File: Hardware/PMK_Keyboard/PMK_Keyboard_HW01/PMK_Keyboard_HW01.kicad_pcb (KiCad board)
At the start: 2 copper layers, 181.6 x 172.3 mm, 151 parts, among them J101 USB4510-03-1-A, J401 Conn_01x08_Female, J402 Conn_01x03_Socket, SW501 SW_Push, SW502 SW_Push, SW503 SW_Push, SW504 SW_Push, SW505 SW_Push, SW506 SW_Push, SW507 SW_Push, SW508 SW_Push, SW509 SW_Push, SW510 SW_Push, SW511 SW_Push, SW512 SW_Push, SW513 SW_Push, SW514 SW_Push, SW515 SW_Push, SW516 SW_Push, SW517 SW_Push, SW518 SW_Push, SW519 SW_Push, SW520 SW_Push, SW521 SW_Push, SW522 SW_Push, SW523 SW_Push, SW524 SW_Push, SW525 SW_Push, SW526 SW_Push, SW527 SW_Push, SW528 SW_Push, SW529 SW_Push, SW530 SW_Push, SW531 SW_Push, SW532 SW_Push, SW533 SW_Push, SW534 SW_Push, SW535 SW_Push, SW536 SW_Push, SW537 SW_Push, SW538 SW_Push, SW539 SW_Push, SW540 SW_Push, U201 BQ24075RGTR, U301 MIC5528-3.3YMT-T5, U302 MIC5528-3.3YMT-T5, U401 ESP32-S2FH4, U501 SN74HC165PWR, U502 SN74HC165PWR, U503 SN74HC165PWR, U504 SN74HC165PWR, U505 SN74HC165PWR, Y601 Crystal_GND24_Small

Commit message: Started routing
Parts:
- removed ANT401: 2450AT18A100E, Component_lib:ANTC3216X140N
- removed BT101: Battery_Cell, Component_lib:BatteryHolder_Keystone_1042_1x18650_DUALSIDE
- removed C201, C203: 4u7, Capacitor_SMD:C_0603_1608Metric
- removed C202: 1u, Capacitor_SMD:C_0603_1608Metric
- removed C301, C302, C303, C304: 2u2, Capacitor_SMD:C_0603_1608Metric
- removed C401, C402: 15p, Capacitor_SMD:C_0201_0603Metric
- removed C403, C404, C405, C408, C411, C412, C414, C415, C416: 100n, Capacitor_SMD:C_0402_1005Metric
- removed C406, C407: C, Capacitor_SMD:C_0201_0603Metric
- removed C409: 10u, Capacitor_SMD:C_0603_1608Metric
- removed C410, C413: 1u, Capacitor_SMD:C_0402_1005Metric
- removed D201, D202: LED, Component_lib:LED_0402_1005Metric_DUALSIDE
- removed D601, D602, D603, D604, D605, D606, D607, D608, D609, D610, D611, D612, D613, D614, D615, D616, D617, D618, D619, D620, D621, D622, D623, D624, D625, D626, D627, D628, D629, D630, D631, D632, D633, D634, D635, D636, D637, D638, D639, D640: YF923_2020_WS2812_LED, Component_lib:YF923_2020_WS2812_LED_DUALSIDE
- removed G*** (x2): LOGO, Component_lib:puma_logo_14mm
- removed G***: LOGO, Component_lib:pmk-v1-noFN_180mm
- removed J401: Conn_01x08_Female, Connector_PinHeader_1.27mm:PinHeader_1x08_P1.27mm_Vertical
- removed J402: Conn_01x03_Socket, Connector_PinHeader_2.54mm:PinHeader_1x03_P2.54mm_Vertical
- removed L401: L, Inductor_SMD:L_0201_0603Metric
- removed R205, R206: 1k5, Resistor_SMD:R_0402_1005Metric
- removed R207: 100k, Resistor_SMD:R_0402_1005Metric
- removed R301: 0k, Resistor_SMD:R_0201_0603Metric
- removed R401: 0, Resistor_SMD:R_0201_0603Metric
- removed R402: 2k, Resistor_SMD:R_0402_1005Metric
- removed R403, R404: 10k, Resistor_SMD:R_0201_0603Metric
- removed R405, R406, R407, R408: nu, Resistor_SMD:R_0201_0603Metric
- removed RN501, RN502, RN503, RN504, RN505: EXB-2HV103JV, Component_lib:EXB2HV_1
- removed S401, S402: SKRPABE010, Component_lib:SKRPABE010
- removed SW501: SW_Push, Component_lib:SKRPABE010
- removed SW502, SW503, SW504, SW505, SW506, SW507, SW508, SW509, SW510, SW511, SW512, SW513, SW514, SW515, SW516, SW517, SW518, SW519, SW520, SW521, SW522, SW523, SW524, SW525, SW526, SW527, SW528, SW529, SW530, SW531, SW532, SW533, SW534, SW535, SW536, SW537, SW538, SW539, SW540: SW_Push, Component_lib:Kailh_socket_PG1350_reversible
- removed TP201: TestPoint, TestPoint:TestPoint_Pad_D1.0mm
- removed U201: BQ24075RGTR, Component_lib:QFN50P300X300X100-17N-D
- removed U401: ESP32-S2FH4, Component_lib:QFN40P700X700X90-57N-D
- removed U501, U502, U503, U504, U505: SN74HC165PWR, Component_lib:SOP65P640X120-16N
- removed Y601: Crystal_GND24_Small, Component_lib:Crystal_SMD_2016-4Pin_2.0x1.6mm
- added D402: YF923_2020_WS2812_LED, Component_lib:YF923_2020_WS2812_LED_DUALSIDE, F.Cu at (43.9, 80.0)
- added D403: YF923_2020_WS2812_LED, Component_lib:YF923_2020_WS2812_LED_DUALSIDE, F.Cu at (43.9, 83.6)
- added D404: YF923_2020_WS2812_LED, Component_lib:YF923_2020_WS2812_LED_DUALSIDE, F.Cu at (43.9, 87.1)
- added D405: YF923_2020_WS2812_LED, Component_lib:YF923_2020_WS2812_LED_DUALSIDE, F.Cu at (43.9, 90.7)
- added D406: YF923_2020_WS2812_LED, Component_lib:YF923_2020_WS2812_LED_DUALSIDE, F.Cu at (43.9, 94.2)
- added D407: YF923_2020_WS2812_LED, Component_lib:YF923_2020_WS2812_LED_DUALSIDE, F.Cu at (43.9, 97.8)
- added D408: YF923_2020_WS2812_LED, Component_lib:YF923_2020_WS2812_LED_DUALSIDE, F.Cu at (43.9, 101.3)
- added D409: YF923_2020_WS2812_LED, Component_lib:YF923_2020_WS2812_LED_DUALSIDE, F.Cu at (43.9, 104.8)
- added D410: YF923_2020_WS2812_LED, Component_lib:YF923_2020_WS2812_LED_DUALSIDE, F.Cu at (48.5, 76.5)
- added D411: YF923_2020_WS2812_LED, Component_lib:YF923_2020_WS2812_LED_DUALSIDE, F.Cu at (48.5, 80.0)
- added D412: YF923_2020_WS2812_LED, Component_lib:YF923_2020_WS2812_LED_DUALSIDE, F.Cu at (48.5, 83.6)
- added D413: YF923_2020_WS2812_LED, Component_lib:YF923_2020_WS2812_LED_DUALSIDE, F.Cu at (48.5, 87.1)
- added D414: YF923_2020_WS2812_LED, Component_lib:YF923_2020_WS2812_LED_DUALSIDE, F.Cu at (48.5, 90.7)
- added D415: YF923_2020_WS2812_LED, Component_lib:YF923_2020_WS2812_LED_DUALSIDE, F.Cu at (48.5, 94.2)
- added D416: YF923_2020_WS2812_LED, Component_lib:YF923_2020_WS2812_LED_DUALSIDE, F.Cu at (48.5, 97.8)
- added D417: YF923_2020_WS2812_LED, Component_lib:YF923_2020_WS2812_LED_DUALSIDE, F.Cu at (48.5, 101.3)
- added D418: YF923_2020_WS2812_LED, Component_lib:YF923_2020_WS2812_LED_DUALSIDE, F.Cu at (48.5, 104.8)
- added D419: YF923_2020_WS2812_LED, Component_lib:YF923_2020_WS2812_LED_DUALSIDE, F.Cu at (53.1, 76.5)
- added D420: YF923_2020_WS2812_LED, Component_lib:YF923_2020_WS2812_LED_DUALSIDE, F.Cu at (53.1, 80.0)
- added D421: YF923_2020_WS2812_LED, Component_lib:YF923_2020_WS2812_LED_DUALSIDE, F.Cu at (53.1, 83.6)
- added D422: YF923_2020_WS2812_LED, Component_lib:YF923_2020_WS2812_LED_DUALSIDE, F.Cu at (53.1, 87.1)
- added D423: YF923_2020_WS2812_LED, Component_lib:YF923_2020_WS2812_LED_DUALSIDE, F.Cu at (53.1, 90.7)
- added D424: YF923_2020_WS2812_LED, Component_lib:YF923_2020_WS2812_LED_DUALSIDE, F.Cu at (53.1, 94.2)
- added D425: YF923_2020_WS2812_LED, Component_lib:YF923_2020_WS2812_LED_DUALSIDE, F.Cu at (53.1, 97.8)
- added D426: YF923_2020_WS2812_LED, Component_lib:YF923_2020_WS2812_LED_DUALSIDE, F.Cu at (53.1, 101.3)
- added D427: YF923_2020_WS2812_LED, Component_lib:YF923_2020_WS2812_LED_DUALSIDE, F.Cu at (53.1, 104.8)
- added D428: YF923_2020_WS2812_LED, Component_lib:YF923_2020_WS2812_LED_DUALSIDE, F.Cu at (57.8, 76.5)
- added D429: YF923_2020_WS2812_LED, Component_lib:YF923_2020_WS2812_LED_DUALSIDE, F.Cu at (57.8, 80.0)
- added D430: YF923_2020_WS2812_LED, Component_lib:YF923_2020_WS2812_LED_DUALSIDE, F.Cu at (57.8, 83.6)
- added D431: YF923_2020_WS2812_LED, Component_lib:YF923_2020_WS2812_LED_DUALSIDE, F.Cu at (57.8, 87.1)
- added D432: YF923_2020_WS2812_LED, Component_lib:YF923_2020_WS2812_LED_DUALSIDE, F.Cu at (57.8, 90.7)
- added J102: PSoM_ESP32S2_Carrier_Board, Component_lib:PSoM_ESP32S2_00, F.Cu at (209.4, 64.8)
- added J201: USB4510-03-1-A, Component_lib:USB4510031A, F.Cu at (209.1, 56.7)
- added J202: Conn_01x05_Pin, Component_lib:SMD_CONN_01x5_1.5mm, B.Cu at (217.4, 89.7)
- added J203: Cirque, Component_lib:Cirque trackpad, F.Cu at (218.8, 89.7)
- added J204: S2B-PH-SM4-TB, Component_lib:JST_PH_B2B-PH-SM4-TB_1x02-1MP_P2.00mm_Vertical_DUALSIDE, F.Cu at (209.2, 89.3)
- added RN301: EXB-2HV103JV, Component_lib:EXB2HV_1, F.Cu at (197.7, 93.6)
- added RN302: EXB-2HV103JV, Component_lib:EXB2HV_1, F.Cu at (197.7, 90.2)
- added RN303: EXB-2HV103JV, Component_lib:EXB2HV_1, F.Cu at (197.7, 86.8)
- added RN304: EXB-2HV103JV, Component_lib:EXB2HV_1, F.Cu at (197.7, 83.4)
- added SW201: 450405020524, Component_lib:450405020524_DUALSIDE, F.Cu at (195.8, 57.5)
- added SW301: RIC11-22S10D5S-TH, Component_lib:RIC11-22S10D5S-TH, F.Cu at (217.1, 126.5)
- added SW302: SW_Push, Component_lib:Kailh_socket_PG1350_reversible, F.Cu at (93.0, 69.1)
- added SW303: SW_Push, Component_lib:Kailh_socket_PG1350_reversible, F.Cu at (112.1, 69.1)
- added SW304: SW_Push, Component_lib:Kailh_socket_PG1350_reversible, F.Cu at (131.1, 64.2)
- added SW305: SW_Push, Component_lib:Kailh_socket_PG1350_reversible, F.Cu at (150.2, 61.4)
- added SW306: SW_Push, Component_lib:Kailh_socket_PG1350_reversible, F.Cu at (169.2, 64.2)
- added SW307: SW_Push, Component_lib:Kailh_socket_PG1350_reversible, F.Cu at (188.3, 66.7)
- added SW308: SW_Push, Component_lib:Kailh_socket_PG1350_reversible, F.Cu at (93.0, 88.2)
- added SW309: SW_Push, Component_lib:Kailh_socket_PG1350_reversible, F.Cu at (112.1, 88.2)
- added SW310: SW_Push, Component_lib:Kailh_socket_PG1350_reversible, F.Cu at (131.1, 83.3)
- added SW311: SW_Push, Component_lib:Kailh_socket_PG1350_reversible, F.Cu at (150.2, 80.8)
- added SW312: SW_Push, Component_lib:Kailh_socket_PG1350_reversible, F.Cu at (169.2, 83.3)
- added SW313: SW_Push, Component_lib:Kailh_socket_PG1350_reversible, F.Cu at (188.3, 85.8)
- added SW314: SW_Push, Component_lib:Kailh_socket_PG1350_reversible, F.Cu at (93.0, 107.2)
- added SW315: SW_Push, Component_lib:Kailh_socket_PG1350_reversible, F.Cu at (112.1, 107.2)
- added SW316: SW_Push, Component_lib:Kailh_socket_PG1350_reversible, F.Cu at (131.1, 102.3)
- added SW317: SW_Push, Component_lib:Kailh_socket_PG1350_reversible, F.Cu at (150.2, 99.8)
- added SW318: SW_Push, Component_lib:Kailh_socket_PG1350_reversible, F.Cu at (169.2, 102.3)
- added SW319: SW_Push, Component_lib:Kailh_socket_PG1350_reversible, F.Cu at (188.3, 104.8)
- added SW320: SW_Push, Component_lib:Kailh_socket_PG1350_reversible, F.Cu at (93.0, 126.3)
- added SW321: SW_Push, Component_lib:Kailh_socket_PG1350_reversible, F.Cu at (112.1, 126.3)
- added SW322: SW_Push, Component_lib:Kailh_socket_PG1350_reversible, F.Cu at (131.1, 121.4)
- added SW323: SW_Push, Component_lib:Kailh_socket_PG1350_reversible, F.Cu at (150.2, 118.9)
- added SW324: SW_Push, Component_lib:Kailh_socket_PG1350_reversible, F.Cu at (169.2, 121.4)
- added SW325: SW_Push, Component_lib:Kailh_socket_PG1350_reversible, F.Cu at (188.3, 123.9)
- added SW326: SW_Push, Component_lib:Kailh_socket_PG1350_reversible, F.Cu at (131.1, 140.4)
- added SW327: SW_Push, Component_lib:Kailh_socket_PG1350_reversible, F.Cu at (150.2, 137.9)
- added SW328: SW_Push, Component_lib:Kailh_socket_PG1350_reversible, F.Cu at (169.2, 140.4)
- added SW329: SW_Push, Component_lib:Kailh_socket_PG1350_reversible, F.Cu at (191.2, 145.1)
- added SW330: SW_Push, Component_lib:Kailh_socket_PG1350_reversible, F.Cu at (212.1, 150.1)
- added TH101: Thermistor_NTC, Resistor_SMD:R_0402_1005Metric, F.Cu at (159.8, 93.8)
- added U303: SN74HC165PWR, Component_lib:SOP65P640X120-16N, F.Cu at (195.8, 112.0)
- added U304: SN74HC165PWR, Component_lib:SOP65P640X120-16N, F.Cu at (195.8, 105.2)
- D401: value LED -> YF923_2020_WS2812_LED; footprint Component_lib:LED_0402_1005Metric_DUALSIDE -> Component_lib:YF923_2020_WS2812_LED_DUALSIDE
- J101: value USB4510-03-1-A -> PSoM_ESP32S2_Carrier_Board; footprint Component_lib:USB4510031A -> Component_lib:PSoM_ESP32S2_00; moved to B.Cu
- R101, R102: value 5.1k -> R; footprint Resistor_SMD:R_0201_0603Metric -> Resistor_SMD:R_0402_1005Metric
- R201: value 0 -> 5.1k; footprint Resistor_SMD:R_0402_1005Metric -> Resistor_SMD:R_0201_0603Metric
- R202: value 36k5 -> 5.1k; footprint Resistor_SMD:R_0402_1005Metric -> Resistor_SMD:R_0201_0603Metric
- R203: value 590 -> 0; footprint Resistor_SMD:R_0402_1005Metric -> Resistor_SMD:R_0201_0603Metric
- R204: value 1k1 -> 0; footprint Resistor_SMD:R_0402_1005Metric -> Resistor_SMD:R_0201_0603Metric
- U301, U302: value MIC5528-3.3YMT-T5 -> SN74HC165PWR; footprint Component_lib:SON40P120X120X60-7N-D -> Component_lib:SOP65P640X120-16N
- moved R203 132.6 mm to (112.0, 143.9)
- moved R204 129.5 mm to (113.3, 145.1), turned to 45 degrees
- moved R202 128.5 mm to (108.3, 140.1)
- moved R201 128.1 mm to (107.1, 138.9)
- moved D401 120.1 mm to (43.9, 76.5), turned to 0 degrees
- moved U302 109.3 mm to (195.8, 118.7), turned to 180 degrees
- moved R101 96.3 mm to (205.5, 88.5), turned to 0 degrees
- moved R102 94.7 mm to (205.5, 90.5), turned to 0 degrees
- moved J101 84.8 mm to (209.3, 64.8), turned to 0 degrees
- moved U301 81.4 mm to (209.5, 73.6), turned to 180 degrees
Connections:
- D401 pad 2: /400- ESP32S2FH4S2/LED_NET -> VDD
- R101 pad 1: /100- Connectors/CC2 -> /100- PSoM/LED_MOSI_ESP
- R101 pad 2: GND -> /100- PSoM/LED_MOSI
- R102 pad 1: /100- Connectors/CC1 -> /100- PSoM/SPI_CLK_ESP
- R102 pad 2: GND -> /100- PSoM/SPI_MISO
- R201 pad 1: /200- 1S_Charger/SYSOFF -> /200- Connectors/CC2
- R202 pad 1: /200- 1S_Charger/TMR -> /200- Connectors/CC1
- R203 pad 1: /200- 1S_Charger/ISET -> Net-(SW201-A)
- R203 pad 2: GND -> /VBAT
- R204 pad 1: GND -> Net-(SW201-C)
- R204 pad 2: /200- 1S_Charger/ILIM -> /VBAT
- U301 pad 1: +3V3 -> /100- PSoM/PL
- U301 pad 2: +3V3 -> /100- PSoM/SPI_CLK
- U301 pad 3: GND -> /300- Shift Register - Switch/4
- U301 pad 4: /300- Power/PRIM_LDO_EN -> /300- Shift Register - Switch/3
- U301 pad 5: unconnected-(U301-NC-Pad5) -> /300- Shift Register - Switch/2
- U301 pad 6: /VSYS -> /300- Shift Register - Switch/1
- U301 pad 7: GND -> unconnected-(U301-~{QH}-Pad7)
- U302 pad 1: VDD -> /100- PSoM/PL
- U302 pad 2: VDD -> /100- PSoM/SPI_CLK
- U302 pad 3: GND -> /300- Shift Register - Switch/12
- U302 pad 4: /300- Power/LED_EN -> /300- Shift Register - Switch/11
- U302 pad 5: unconnected-(U302-NC-Pad5) -> /300- Shift Register - Switch/10
- U302 pad 6: /VSYS -> /300- Shift Register - Switch/9
- U302 pad 7: GND -> unconnected-(U302-~{QH}-Pad7)
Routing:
- net VDD: track 1246.0 -> 0.00 mm, vias 53 -> 0
- net GND: track 388.5 -> 0.00 mm, vias 151 -> 0
- net +3V3: track 227.7 -> 0.00 mm, vias 19 -> 0
- net /500- Shift Register - Switch/18: track 178.7 -> 0.00 mm, vias 2 -> 0
- net /400- ESP32S2FH4S2/SR_CLK: track 176.9 -> 0.00 mm, vias 7 -> 0
- net /500- Shift Register - Switch/17: track 174.3 -> 0.00 mm, vias 2 -> 0
- net /400- ESP32S2FH4S2/SR_CS: track 173.7 -> 0.00 mm, vias 8 -> 0
- net /500- Shift Register - Switch/10: track 172.6 -> 0.00 mm, vias 4 -> 0
- net /500- Shift Register - Switch/25: track 170.7 -> 0.00 mm, vias 2 -> 0
- net /400- ESP32S2FH4S2/PL: track 158.6 -> 0.00 mm, vias 7 -> 0
- net /500- Shift Register - Switch/2: track 158.4 -> 0.00 mm, vias 2 -> 0
- net /500- Shift Register - Switch/9: track 156.5 -> 0.00 mm, vias 2 -> 0
- net /500- Shift Register - Switch/27: track 155.4 -> 0.00 mm, vias 2 -> 0
- net /500- Shift Register - Switch/26: track 154.3 -> 0.00 mm, vias 2 -> 0
- net /500- Shift Register - Switch/19: track 134.6 -> 0.00 mm, vias 2 -> 0
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- removed copper zone on B.Cu, net +3V3
- removed copper zone on F.Cu, net +3V3
- removed copper zone on F.Cu, net /VSYS
- removed copper zone on B.Cu, net GND
- removed copper zone on F.Cu, net GND
- removed copper zone on F.Cu, net VDD
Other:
- board size 181.6 x 172.3 mm -> 143.4 x 111.7 mm
- board text added: "+"
- board text added: "-"
- board text added: "Sofle Choc Wireless - revision by db"
- board text added: "s1"
- board text added: "s10"
- board text added: "s11"
- board text added: "s12"
- board text added: "s13"
- board text added: "s14"
- board text added: "s15"
- board text added: "s16"
- board text added: "s17"
- board text added: "s18"
- board text added: "s19"
- board text added: "s2"
- board text added: "s20"
- board text added: "s21"
- board text added: "s22"
- board text added: "s23"
- board text added: "s24"
- board text added: "s25"
- board text added: "s26"
- board text added: "s27"
- board text added: "s28"
- board text added: "s29"
- board text added: "s3"
- board text added: "s30"
- board text added: "s4"
- board text added: "s5"
- board text added: "s6"
- board text added: "s7"
- board text added: "s8"
- board text added: "s9"
- board text removed: "PMK_KEYBOARD_HW00"

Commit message: working on routing
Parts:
- removed D430, D431, D432: YF923_2020_WS2812_LED, Component_lib:YF923_2020_WS2812_LED_DUALSIDE
- removed the SW301 at (217.1, 126.5)
- added SW330: RIC11-22S10D5S-TH, Component_lib:RIC11-22S10D5S-TH, F.Cu at (214.8, 126.8)
- J202: moved to F.Cu
- J203, RN301, RN302, RN303, RN304: moved to B.Cu
- J204: footprint Component_lib:JST_PH_B2B-PH-SM4-TB_1x02-1MP_P2.00mm_Vertical_DUALSIDE -> Component_lib:JST_PH_S2B-PH-SM4-TB_1x02-1MP_P2.00mm_Horizontal_DUALSIDE; moved to B.Cu
- moved D425 160.5 mm to (205.7, 147.7), turned to 60 degrees
- moved D401 142.8 mm to (185.9, 61.8)
- moved D426 142.2 mm to (189.9, 140.3), turned to -15 degrees
- moved D413 138.0 mm to (185.9, 100.0)
- moved D412 137.4 mm to (185.9, 80.9), turned to 180 degrees
- moved D424 135.1 mm to (185.9, 119.0), turned to 180 degrees
- moved R202 125.4 mm to (207.0, 62.8), turned to -90 degrees
- moved R204 125.1 mm to (218.2, 77.0), turned to 180 degrees
- moved D402 124.7 mm to (166.9, 59.3)
- moved R203 124.4 mm to (218.2, 79.0), turned to 180 degrees
- moved R201 124.2 mm to (205.3, 62.8), turned to -90 degrees
- moved D414 118.5 mm to (166.8, 97.5)
- moved D411 118.4 mm to (166.9, 78.4), turned to 180 degrees
- moved D427 117.8 mm to (166.9, 135.5)
- moved D423 116.7 mm to (166.9, 116.5), turned to 180 degrees
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- renumbered SW302 to SW301, SW303 to SW302, SW304 to SW303, SW305 to SW304, SW306 to SW305, SW307 to SW306, SW308 to SW307, SW309 to SW308, SW310 to SW309, SW311 to SW310, SW312 to SW311, SW313 to SW312, SW314 to SW313, SW315 to SW314, SW316 to SW315, SW317 to SW316, SW318 to SW317, SW319 to SW318, SW320 to SW319, SW321 to SW320, SW322 to SW321, SW323 to SW322, SW324 to SW323, SW325 to SW324, SW326 to SW325, SW327 to SW326, SW328 to SW327, SW329 to SW328, SW330 to SW329
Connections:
- D429 pad 4: Net-(D429-DO) -> unconnected-(D429-DO-Pad4)
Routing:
- net VDD: track 0.00 -> 705.3 mm, vias 0 -> 29
- net Net-(D425-DO): track 0.00 -> 25.1 mm
- net /400- LEDs/LED_26_27: track 0.00 -> 23.5 mm, vias 0 -> 2
- net Net-(D412-DO): track 0.00 -> 22.3 mm
- net Net-(D406-DO): track 0.00 -> 20.6 mm
- net Net-(D416-DO): track 0.00 -> 19.1 mm
- net Net-(D408-DO): track 0.00 -> 19.1 mm
- net Net-(D420-DO): track 0.00 -> 19.0 mm
- net Net-(D404-DO): track 0.00 -> 19.0 mm
- net Net-(D402-DO): track 0.00 -> 18.9 mm
- net Net-(D427-DO): track 0.00 -> 18.8 mm
- net /400- LEDs/LED_13_14: track 0.00 -> 18.8 mm, vias 0 -> 2
- net Net-(D411-DO): track 0.00 -> 18.7 mm, vias 0 -> 2
- net Net-(D410-DO): track 0.00 -> 18.7 mm
- net Net-(D423-DO): track 0.00 -> 18.7 mm, vias 0 -> 2
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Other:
- board size 143.4 x 111.7 mm -> 145 x 111.8 mm
- board text removed: "+"
- board text removed: "-"

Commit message: led routing
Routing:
- net Net-(D424-DO): track 0.00 -> 54.2 mm, vias 0 -> 4
- net Net-(D418-DO): track 0.00 -> 24.7 mm, vias 0 -> 2
- net Net-(D428-DO): track 18.0 -> 23.5 mm, vias 0 -> 2
- net Net-(D412-DO): track 22.3 -> 26.8 mm, vias 0 -> 2
- net Net-(D425-DO): track 25.1 -> 29.4 mm, vias 0 -> 2
- net Net-(D421-DO): track 18.1 -> 22.4 mm, vias 0 -> 2
- net Net-(D409-DO): track 18.1 -> 22.3 mm, vias 0 -> 2
- net Net-(D404-DO): track 19.0 -> 23.2 mm, vias 0 -> 2
- net Net-(D403-DO): track 18.1 -> 22.3 mm, vias 0 -> 2
- net Net-(D415-DO): track 18.0 -> 22.1 mm, vias 0 -> 2
- net Net-(D416-DO): track 19.1 -> 23.1 mm, vias 0 -> 2
- net Net-(D406-DO): track 20.6 -> 24.2 mm, vias 0 -> 2
- net /400- LEDs/LED_13_14: track 18.8 -> 22.2 mm, vias 2 -> 4
- net Net-(D405-DO): track 17.7 -> 21.2 mm, vias 0 -> 2
- net Net-(D420-DO): track 19.0 -> 22.4 mm, vias 0 -> 2
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
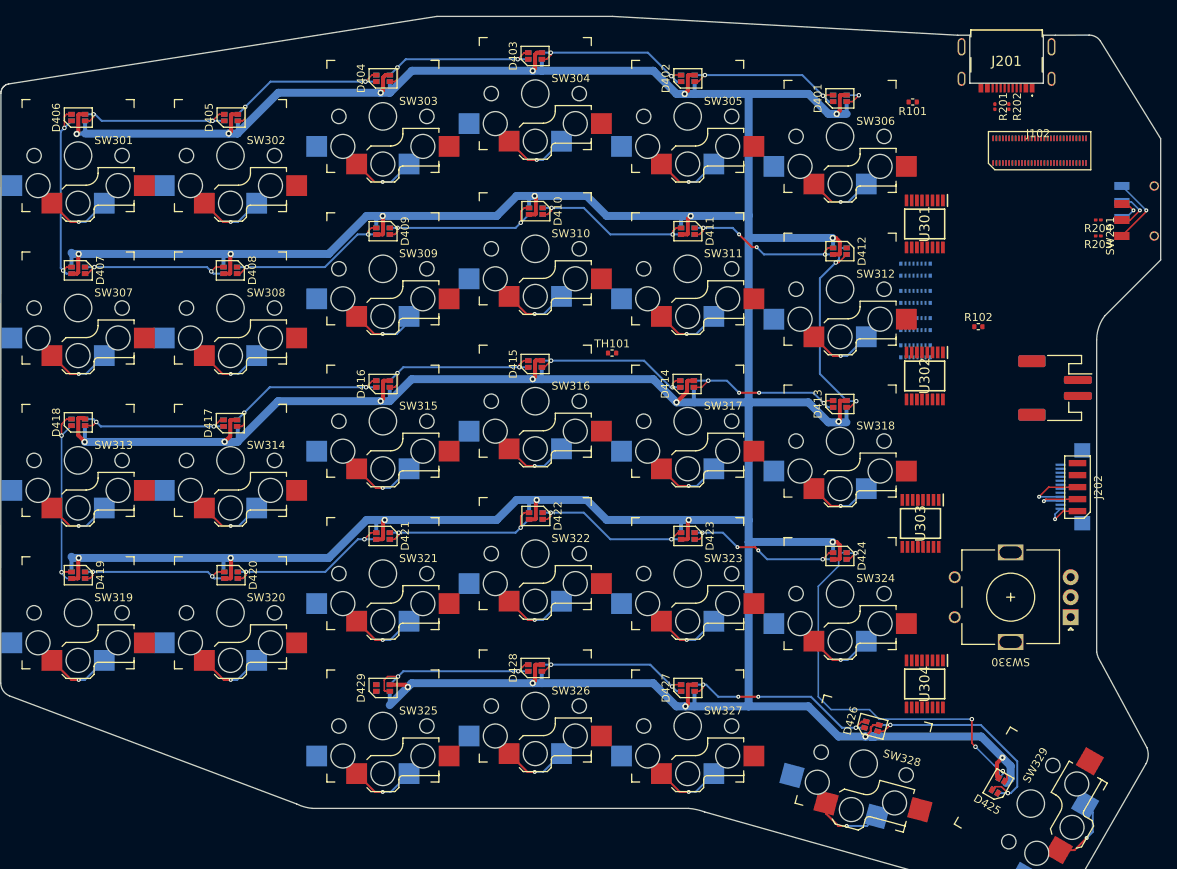
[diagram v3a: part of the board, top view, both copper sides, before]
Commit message: Need to route Shift registers
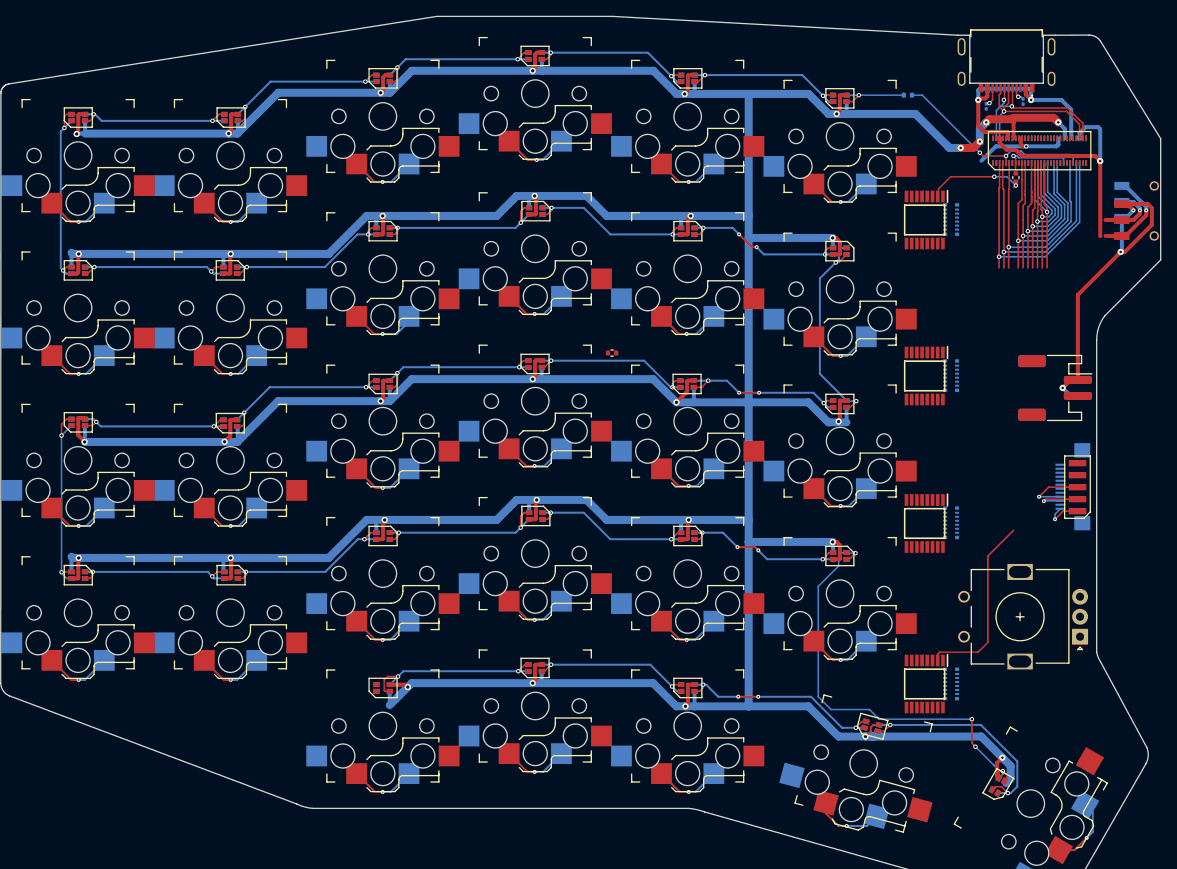
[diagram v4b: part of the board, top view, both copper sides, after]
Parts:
- R101, R201, R202: moved to B.Cu
- moved RN304 52.0 mm to (199.8, 135.0), turned to -90 degrees
- moved RN303 28.6 mm to (199.8, 114.8), turned to -90 degrees
- moved R102 19.2 mm to (207.9, 71.7), turned to -90 degrees
- moved RN301 17.1 mm to (199.8, 77.0), turned to -90 degrees
- moved RN302 7.83 mm to (199.8, 96.5), turned to -90 degrees
- moved SW330 2.72 mm to (215.9, 129.2)
- moved R202 1.89 mm to (208.8, 62.2)
- moved R201 1.07 mm to (204.2, 62.8)
- moved R101 1.04 mm to (194.4, 61.4)
- moved R203 0.60 mm to (218.8, 79.0)
- moved R204 0.60 mm to (218.8, 77.0)
- moved U303 0.53 mm to (196.5, 114.9)
- moved U301 0.50 mm to (196.5, 77.0)
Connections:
- J101 pad 31: unconnected-(J101-IO15-Pad31) -> /100- PSoM/A
- J101 pad 33: unconnected-(J101-IO16-Pad33) -> /100- PSoM/B
- J101 pad 9: /100- PSoM/LED_MOSI -> /100- PSoM/LED_MOSI_ESP
- J102 pad 31: unconnected-(J102-IO15-Pad31) -> /100- PSoM/A
- J102 pad 33: unconnected-(J102-IO16-Pad33) -> /100- PSoM/B
- J102 pad 9: /100- PSoM/LED_MOSI -> /100- PSoM/LED_MOSI_ESP
- R102 pad 2: /100- PSoM/SPI_MISO -> /100- PSoM/SPI_CLK
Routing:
- net Net-(J204-Pin_1): track 3.62 -> 43.0 mm, vias 1 -> 3
- net VDD: track 703.4 -> 739.3 mm, vias 29 -> 33
- net /100- PSoM/SPI_CLK: track 0.00 -> 35.6 mm, vias 0 -> 2
- net /100- PSoM/SPI_MOSI: track 0.00 -> 32.4 mm, vias 0 -> 1
- net /VBAT: track 0.00 -> 32.1 mm, vias 0 -> 1
- net /100- PSoM/SPI_MISO: track 0.00 -> 31.1 mm, vias 0 -> 1
- net VBUS: track 0.00 -> 30.4 mm, vias 0 -> 2
- net /100- PSoM/PL: track 0.00 -> 29.7 mm, vias 0 -> 1
- net /100- PSoM/SR_CE: track 0.00 -> 28.5 mm, vias 0 -> 1
- net /100- PSoM/SDA: track 6.40 -> 33.4 mm, vias 1 -> 2
- net /100- PSoM/GP_CE: track 0.00 -> 26.9 mm, vias 0 -> 1
- net /100- PSoM/LED_MOSI_ESP: track 0.00 -> 25.4 mm, vias 0 -> 2
- net /100- PSoM/SCL: track 7.97 -> 32.5 mm, vias 1 -> 2
- net /100- PSoM/INT: track 0.00 -> 23.0 mm, vias 0 -> 1
- net /100- PSoM/D-: track 0.00 -> 22.1 mm, vias 0 -> 2
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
